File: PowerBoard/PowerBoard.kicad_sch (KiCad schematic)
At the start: 29 parts, among them IC1 ACS37010LLZATR-050B5, IC2 TLF80511TFV50ATMA1, J1 Screw_Terminal_01x02, J2 Screw_Terminal_01x02, J3 Conn_01x04, J4 Conn_ARM_JTAG_SWD_10, U2 STM32L100C6Ux

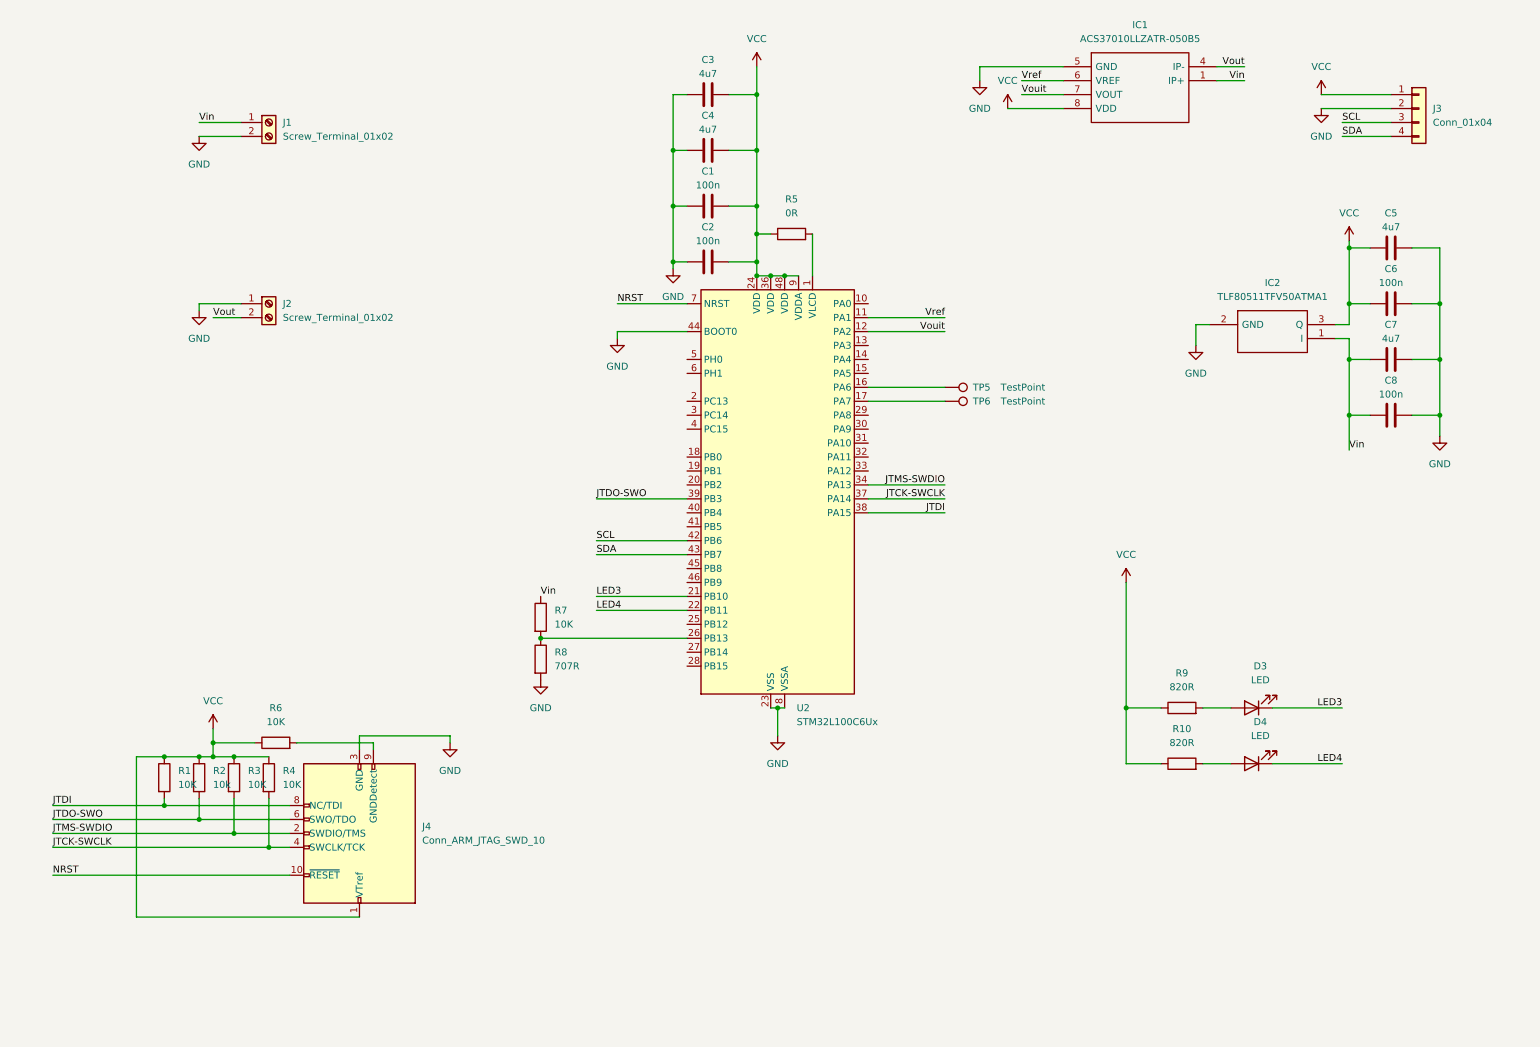
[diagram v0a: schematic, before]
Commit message: Updated the schematic and removed gerber files from project
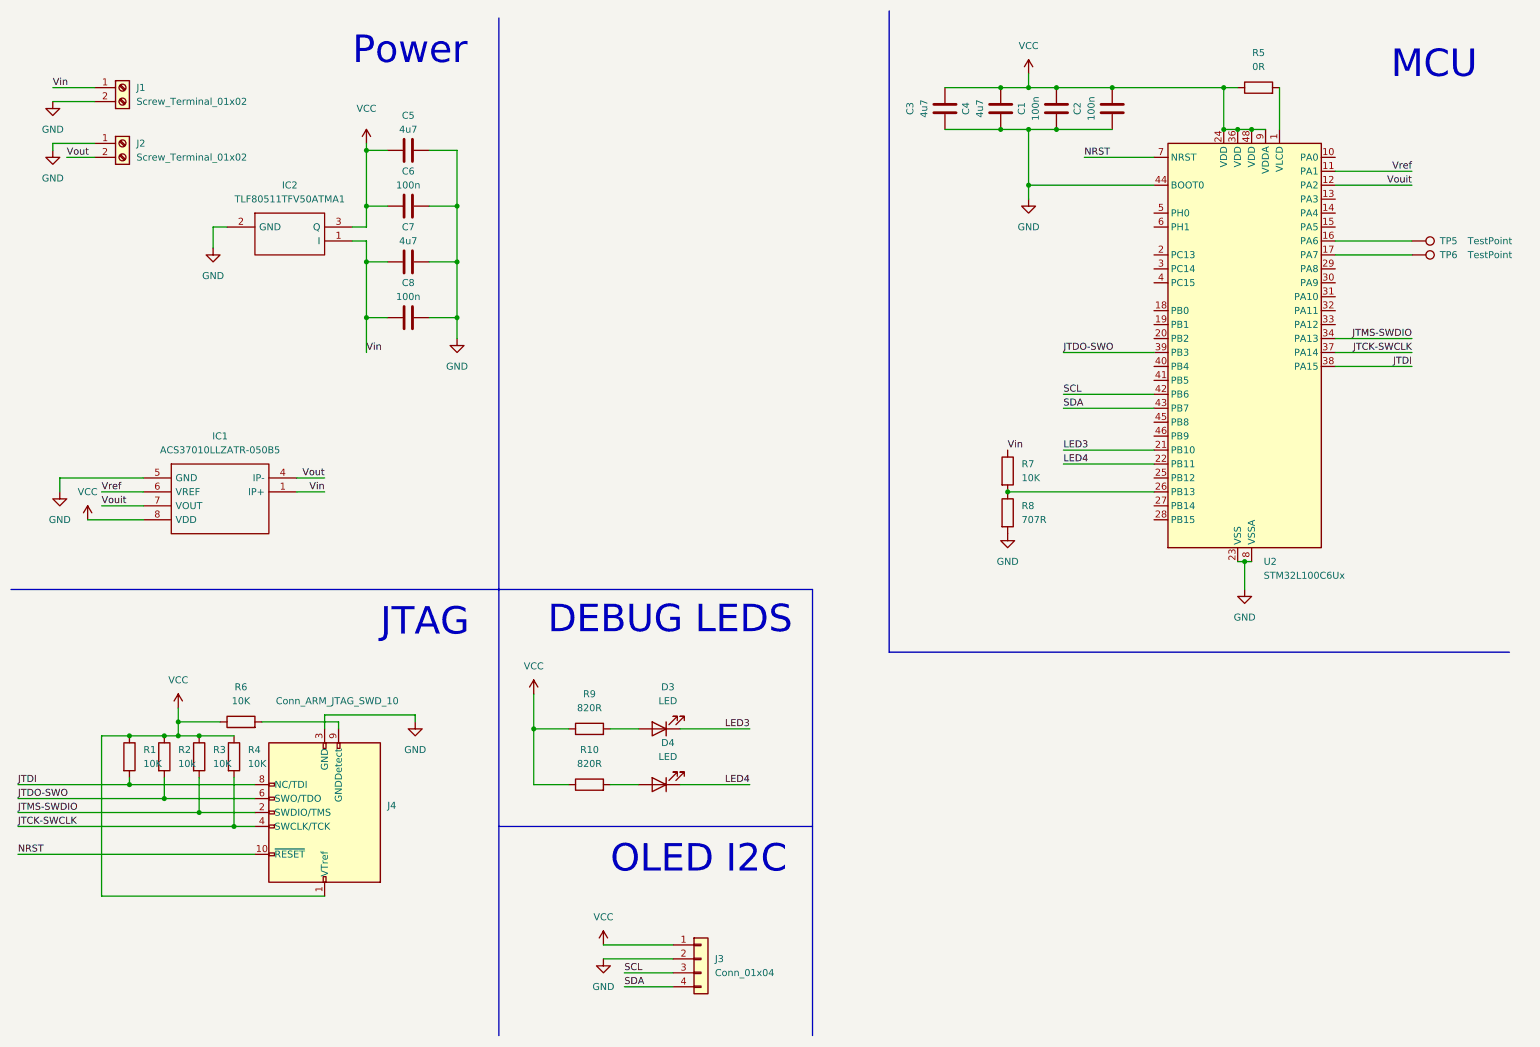
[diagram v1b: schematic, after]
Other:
- note added: "DEBUG LEDS"
- note added: "JTAG"
- note added: "MCU"
- note added: "OLED I2C"
- note added: "Power"
- moved on the sheet: C1, C2, C3, C4, C5, C6, C7, C8, D3, D4, IC1, IC2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
